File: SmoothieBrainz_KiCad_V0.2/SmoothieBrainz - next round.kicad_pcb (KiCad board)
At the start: 2 copper layers, 100 x 80 mm, 127 parts, among them IC1 LPC1769, IC5 LD117ADT33TR, Q1 BSL207SP, Q2 12MHz, SW1 SW_TACT_4P_B, SW3 SW_TACT_4P_B, U2 HC_05, U3 USD-SOCKETUSD, X14 USBPTH

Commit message: More Clean up of Sch
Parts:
- C15, C16, D10, D11, D12, D7, D8, D9, L1, LED1, LED2, LED3, LED4, LED5, LED9: value (none) -> ~
- D2: value (none) -> 214AC
- JP1: value (none) -> JP1
- JP10, JP11, JP12, JP13, JP14, JP15, JP16, JP6, JP7, JP8, JP9: value (none) -> M01
- JP3: value (none) -> SPARKFUN-CONNECTORS_M08
- JP5, SJ1: value (none) -> 1
- S1: value (none) -> sw1
- S2: value (none) -> sw2
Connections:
- net N$23 renamed /N$23
- net RX_FT renamed /RX_FT
- net TX_FT renamed /TX_FT
- C1 pad 2: 3.3V -> +3V3
- C10 pad 2: 3.3V -> +3V3
- C11 pad 2: 3.3V -> +3V3
- C12 pad 2: 3.3V -> +3V3
- C13 pad 2: 3.3V -> +3V3
- C14 pad 2: 3.3V -> +3V3
- C16 pad +: 3.3V -> +3V3
- C17 pad 2: X_MIN -> /X_MIN
- C18 pad 2: X_MAX -> /X_MAX
- C19 pad 2: Y_MIN -> /Y_MIN
- C2 pad 1: N$1 -> /N$1
- C20 pad 2: Y_MAX -> /Y_MAX
- C21 pad 2: Z_MIN -> /Z_MIN
- C22 pad 2: Z_MAX -> /Z_MAX
- C23 pad 1: TH1_HOTEND -> /TH1_HOTEND
- C23 pad 2: AGND -> GND
- C24 pad 1: TH2_BED -> /TH2_BED
- C24 pad 2: AGND -> GND
- C25 pad 1: TH3 -> /TH3
- C25 pad 2: AGND -> GND
- C26 pad +: 24V -> /24V
- C27 pad +: 5VREG -> 5vreg
- C28 pad 1: 12 -> /12
- C28 pad 2: RESET -> /RESET
- C3 pad 1: N$2 -> /N$2
- C4 pad 2: USB_D- -> /USB_D-
- C44 pad 1: 3.3V -> +3V3
- C5 pad 2: USB_D+ -> /USB_D+
- C6 pad 1: AVCC -> /AVCC
- C6 pad 2: AGND -> GND
- C65 pad 1: 3.3V -> +3V3
- C67 pad 2: 3.3V -> +3V3
- C7 pad 1: 3.3V -> +3V3
- C8 pad 2: 3.3V -> +3V3
- C9 pad 2: 3.3V -> +3V3
- D10 pad 1: N$12 -> /N$12
- D10 pad 2: Y_MAX -> /Y_MAX
- D11 pad 1: N$15 -> /N$15
- D11 pad 2: Z_MIN -> /Z_MIN
- D12 pad 1: N$16 -> /N$16
- D12 pad 2: Z_MAX -> /Z_MAX
- D2 pad 1: N$9 -> /N$9
- D3 pad A: 5VREG -> 5vreg
- D7 pad 1: N$6 -> /N$6
- D7 pad 2: X_MIN -> /X_MIN
- D8 pad 1: N$8 -> /N$8
- D8 pad 2: X_MAX -> /X_MAX
- D9 pad 1: N$10 -> /N$10
- D9 pad 2: Y_MIN -> /Y_MIN
- EXP1 pad 9: /GND -> GND
- EXP2 pad 9: /GND -> GND
- IC1 pad 11: /AGND -> GND
- IC1 pad 15: /AGND -> GND
- IC1 pad 19: /3.3V -> +3V3
- IC1 pad 28: /3.3V -> +3V3
- IC1 pad 31: /GND -> GND
- IC1 pad 41: /GND -> GND
- IC1 pad 42: /3.3V -> +3V3
- IC1 pad 54: /3.3V -> +3V3
- IC1 pad 55: /GND -> GND
- IC1 pad 71: /3.3V -> +3V3
- IC1 pad 72: /GND -> GND
- IC1 pad 83: /GND -> GND
- IC1 pad 84: /3.3V -> +3V3
- IC1 pad 96: /3.3V -> +3V3
- IC1 pad 97: /GND -> GND
- IC2 pad 3: /GND -> GND
- IC2 pad 4: /5VREG -> 5vreg
- IC2 pad 5: /GND -> GND
- IC2 pad 6: /GND -> GND
- IC5 pad 1: /GND -> GND
- IC5 pad 4: /3.3V -> +3V3
- IC7 pad 3: /GND -> GND
- IC7 pad 5: /3.3V -> +3V3
- JP1 pad 1: 3.3V -> +3V3
- JP1 pad 10: ENET_RXD0 -> /ENET_RXD0
- JP1 pad 11: ENET_TXD0 -> /ENET_TXD0
- JP1 pad 12: ENET_TX_EN -> /ENET_TX_EN
- JP1 pad 13: (no net) -> Net-(JP1-Pad13)
- JP1 pad 14: ENET_TXD1 -> /ENET_TXD1
- JP1 pad 2: 3.3V -> +3V3
- JP1 pad 5: ENET_MDC -> /ENET_MDC
- JP1 pad 6: ENET_MDIO -> /ENET_MDIO
- JP1 pad 7: ENET_CRS -> /ENET_CRS
- JP1 pad 8: N$77 -> /N$77
- JP1 pad 9: ENET_RXD1 -> /ENET_RXD1
- JP2 pad 27: /5VREG -> 5vreg
- JP2 pad 28: /GND -> GND
- JP2 pad 29: /GND -> GND
- JP2 pad 30: /GND -> GND
- JP3 pad 1: JTAG-RTCK -> /JTAG-RTCK
- JP3 pad 2: RESET -> /RESET
- JP3 pad 3: RSTOUT -> /RSTOUT
- JP3 pad 4: JTAG-TCK -> /JTAG-TCK
- JP3 pad 5: JTAG-TRST -> /JTAG-TRST
- JP3 pad 6: JTAG-TMS -> /JTAG-TMS
- JP3 pad 7: JTAG-TDI -> /JTAG-TDI
- JP3 pad 8: JTAG-TDO -> /JTAG-TDO
- JP5 pad 1: RTS -> /RTS
- L1 pad 1: AVCC -> /AVCC
- L1 pad 2: 3.3V -> +3V3
- L2 pad 1: N$9 -> /N$9
- L2 pad 2: 5VREG -> 5vreg
- LED1 pad A: N$87 -> (no net)
- LED1 pad C: GND -> (no net)
- LED2 pad A: N$86 -> (no net)
- LED2 pad C: GND -> (no net)
- LED3 pad A: N$85 -> (no net)
- LED3 pad C: GND -> (no net)
- LED4 pad A: N$84 -> (no net)
- LED4 pad C: GND -> (no net)
- LED5 pad A: N$3 -> (no net)
- LED5 pad C: GND -> (no net)
- LED9 pad A: N$80 -> (no net)
- LED9 pad C: GND -> (no net)
- Q1 pad 4: /3.3V -> +3V3
- Q2 pad 1: N$2 -> /N$2
- Q2 pad 2: N$1 -> /N$1
- R1 pad 1: SD_CS -> /SD_CS
- R1 pad 2: 3.3V -> +3V3
- R10 pad 1: N$87 -> /N$87
- R10 pad 2: LED1 -> /LED1
- R11 pad 1: N$86 -> /N$86
- R11 pad 2: LED2 -> /LED2
- R12 pad 1: N$85 -> /N$85
- R12 pad 2: LED3 -> /LED3
- R13 pad 1: N$84 -> /N$84
- R13 pad 2: LED4 -> /LED4
- R14 pad 1: RESET -> /RESET
- R14 pad 2: 3.3V -> +3V3
- R15 pad 1: ISP_BOOT -> /ISP_BOOT
- R15 pad 2: 3.3V -> +3V3
- R16 pad 1: RTS -> /RTS
- R16 pad 2: 3.3V -> +3V3
- R17 pad 1: PLAY -> /PLAY
- R17 pad 2: 3.3V -> +3V3
- R18 pad 1: N$3 -> /N$3
- R18 pad 2: PLAY_LED -> /PLAY_LED
- R2 pad 1: SD_MISO -> /SD_MISO
- R2 pad 2: 3.3V -> +3V3
- R21 pad 1: 3.3V -> +3V3
- R21 pad 2: Y_MAX -> /Y_MAX
- R22 pad 1: 3.3V -> +3V3
- R22 pad 2: Y_MIN -> /Y_MIN
- R23 pad 1: 3.3V -> +3V3
- R23 pad 2: X_MAX -> /X_MAX
- R24 pad 1: 3.3V -> +3V3
- R24 pad 2: X_MIN -> /X_MIN
- R28 pad 1: 3.3V -> +3V3
- R28 pad 2: N$18 -> /N$18
- R29 pad 1: 3.3V -> +3V3
- R29 pad 2: RESET1 -> /RESET1
- R3 pad 1: SD_MOSI -> /SD_MOSI
- R3 pad 2: 3.3V -> +3V3
- R31 pad 1: 15 -> /15
- R4 pad 1: 2 -> /2
- R4 pad 2: 3.3V -> +3V3
- R5 pad 1: 3.3V -> +3V3
- R5 pad 2: Z_MAX -> /Z_MAX
- R51 pad 1: N$78 -> /N$78
- R51 pad 2: ENET_REF_CLK -> /ENET_REF_CLK
- R6 pad 1: 3.3V -> +3V3
- R6 pad 2: Z_MIN -> /Z_MIN
- R7 pad 1: USB_D+ -> /USB_D+
- R7 pad 2: N$51 -> /N$51
- R77 pad 1: N$80 -> /N$80
- R77 pad 2: 3.3V -> +3V3
- R8 pad 1: N$61 -> /N$61
- R8 pad 2: USB_D+ -> /USB_D+
- R9 pad 1: N$62 -> /N$62
- R9 pad 2: USB_D- -> /USB_D-
- RN1 pad 1: AVCC -> /AVCC
- RN1 pad 2: AVCC -> /AVCC
- RN1 pad 3: AVCC -> /AVCC
- RN1 pad 6: TH3 -> /TH3
- RN1 pad 7: TH2_BED -> /TH2_BED
- RN1 pad 8: TH1_HOTEND -> /TH1_HOTEND
- S1 pad 1: RESET -> (no net)
- S1 pad 2: RESET -> (no net)
- S1 pad 3: GND -> (no net)
- S1 pad 4: GND -> (no net)
- S2 pad 1: ISP_BOOT -> (no net)
- S2 pad 2: ISP_BOOT -> (no net)
- S2 pad 3: GND -> (no net)
- S2 pad 4: GND -> (no net)
- SJ1 pad 1: 3.3V -> +3V3
- SJ2 pad 2: RX_0 -> /RX_0
- SJ3 pad 2: TX_0 -> /TX_0
- SJ4 pad 2: ESPTX -> /ESPTX
- SJ5 pad 2: ESPRX -> /ESPRX
- SJ6 pad 1: RX_0 -> /RX_0
- SJ6 pad 2: ESPTX -> /ESPTX
- SJ7 pad 1: TX_0 -> /TX_0
- SJ7 pad 2: ESPRX -> /ESPRX
- SW1 pad 2: /GND -> GND
- SW3 pad 2: /GND -> GND
- U$2 pad 1: /GND -> GND
- U$2 pad 16: /3.3V -> +3V3
- U2 pad 12: /3.3V -> +3V3
- U2 pad 13: /GND -> GND
- U3 pad 1: (no net) -> Net-(U3-Pad1)
- U3 pad 2: SD_CS -> /SD_CS
- U3 pad 3: SD_MOSI -> /SD_MOSI
- U3 pad 4: 3.3V -> +3V3
- U3 pad 5: SD_SCK -> /SD_SCK
- U3 pad 7: SD_MISO -> /SD_MISO
- U3 pad 8: (no net) -> Net-(U3-Pad8)
- U3 pad CD1: (no net) -> GND
- U3 pad CD2: (no net) -> GND
- U3 pad GND2: GND -> (no net)
- VP_0 pad VP: /GND -> GND
- VP_1 pad VP: /GND -> GND
- VP_2 pad VP: /GND -> GND
- VP_3 pad VP: /GND -> GND
- VP_4 pad VP: /GND -> GND
- X1 pad 2: /AGND -> GND
- X1 pad 4: /AGND -> GND
- X1 pad 6: /AGND -> GND
- X14 pad D+: N$61 -> /N$62
- X14 pad D-: N$62 -> /N$61
- X14 pad GND: GND -> VUSB
- X14 pad VBUS: VUSB -> GND
- XMN88 pad 2: /GND -> GND
- XMX88 pad 2: /GND -> GND
- YMN88 pad 2: /GND -> GND
- YMX88 pad 2: /GND -> GND
- ZMN88 pad 2: /GND -> GND
- ZMX88 pad 2: /GND -> GND
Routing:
- net +3V3: track 0.00 -> 540.1 mm, vias 0 -> 22
- net GND: track 453.7 -> 904.7 mm, vias 34 -> 76
- net 3.3V: track 400.5 -> 0.00 mm, vias 16 -> 0
- net /GND: track 374.2 -> 0.00 mm, vias 34 -> 0
- net /3.3V: track 139.6 -> 0.00 mm, vias 6 -> 0
- net 5vreg: track 0.00 -> 74.9 mm, vias 0 -> 1
- net RESET: track 64.9 -> 0.00 mm, vias 2 -> 0
- net /RESET: track 34.0 -> 98.9 mm, vias 4 -> 6
- net 5VREG: track 52.7 -> 0.00 mm, vias 1 -> 0
- net Z_MAX: track 51.3 -> 0.00 mm
- net /Z_MAX: track 18.6 -> 69.9 mm
- net AGND: track 48.8 -> 0.00 mm, vias 6 -> 0
- net PLAY: track 41.7 -> 0.00 mm, vias 3 -> 0
- net /PLAY: track 26.4 -> 68.1 mm, vias 3 -> 6
- net Z_MIN: track 38.9 -> 0.00 mm
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
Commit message: More Cleaning up
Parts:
- X14: value USBPTH -> USB; footprint USB-B-PTH -> SmoothieBrainz - next round:SPARKFUN_USB-B-PTH
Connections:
- X14 pad D+: /N$62 -> /N$61
- X14 pad D-: /N$61 -> /N$62
- X14 pad GND: VUSB -> GND
- X14 pad VBUS: GND -> VUSB
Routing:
- net VUSB: track 3.59 -> 15.6 mm, vias 0 -> 2
- net GND: track 904.7 -> 892.7 mm, vias 76 -> 74
- net /N$61: track 8.85 -> 7.34 mm
- net /N$62: track 3.51 -> 5.02 mm

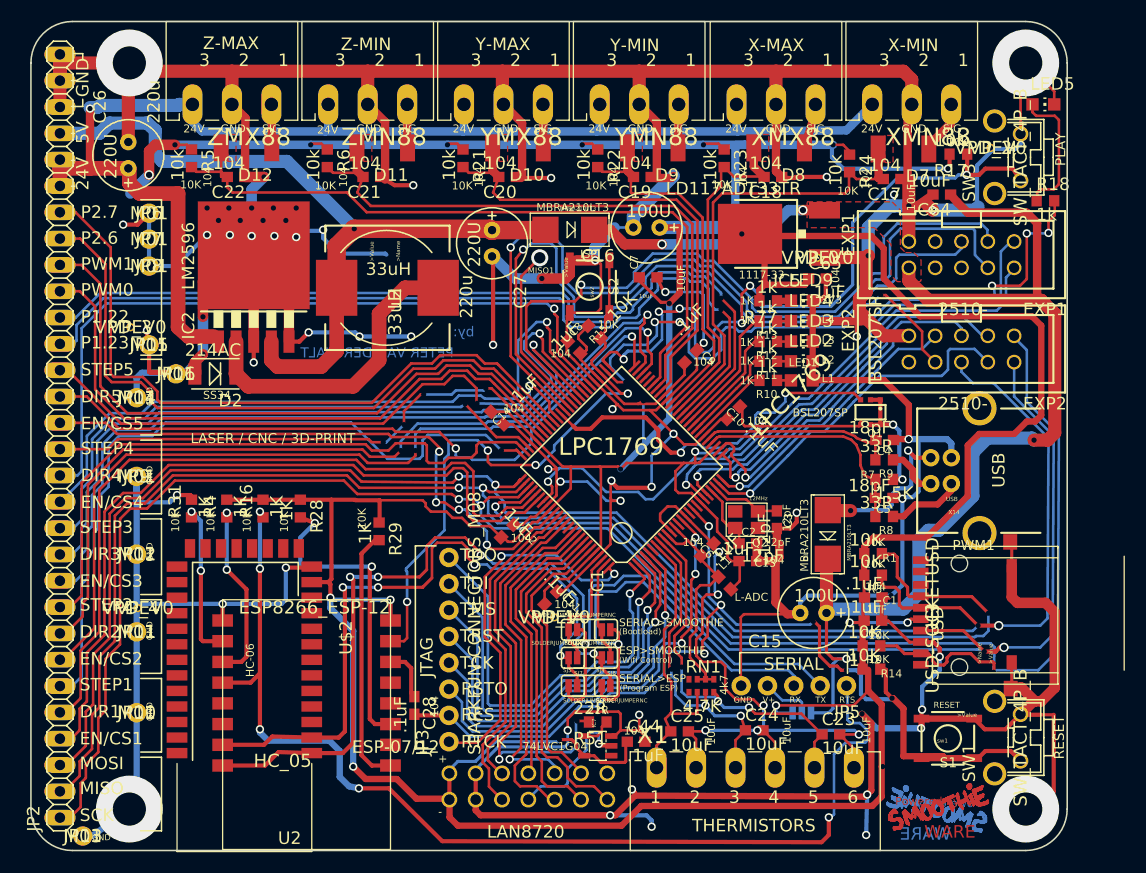
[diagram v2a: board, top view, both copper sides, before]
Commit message: More PCB Clean up Started to resize under size vias
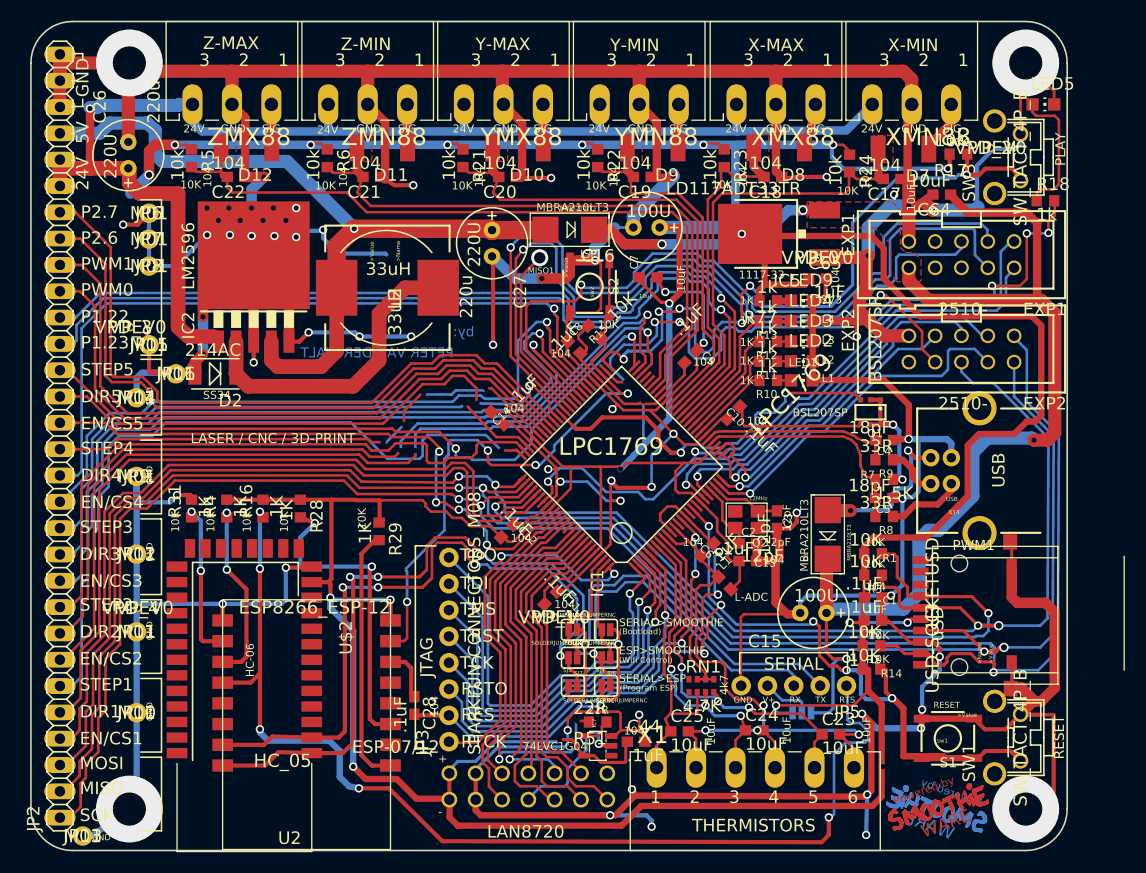
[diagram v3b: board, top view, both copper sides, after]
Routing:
- added copper zone on F.Cu, net /X_MAX
- added copper zone on F.Cu, net /X_MIN
- added copper zone on F.Cu, net /Y_MAX
- added copper zone on F.Cu, net /Y_MIN
- added copper zone on F.Cu, net /Z_MAX
- added copper zone on F.Cu, net /Z_MIN
